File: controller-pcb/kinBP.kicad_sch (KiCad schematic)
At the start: 33 parts, among them J1 LEFT_TOP, J10 LEFT_THUMB, J11 RIGHT_THUMB, J12 RIGHT_THUMB, J13 LEFT_THUMB, J14 Conn_02x04_Odd_Even, J15 USB Cable Socket, J2 LEFT_TOP, J3 RIGHT_TOP, J4 RIGHT_TOP, J5 RIGHT_KEYWELL, J6 LEFT_KEYWELL, J7 LEFT_THUMB, J8 RIGHT_THUMB, J9 Conn_02x04_Odd_Even, Q1 MMBT3904, Q2 MMBT3904, U1 weact_STM32F4x1

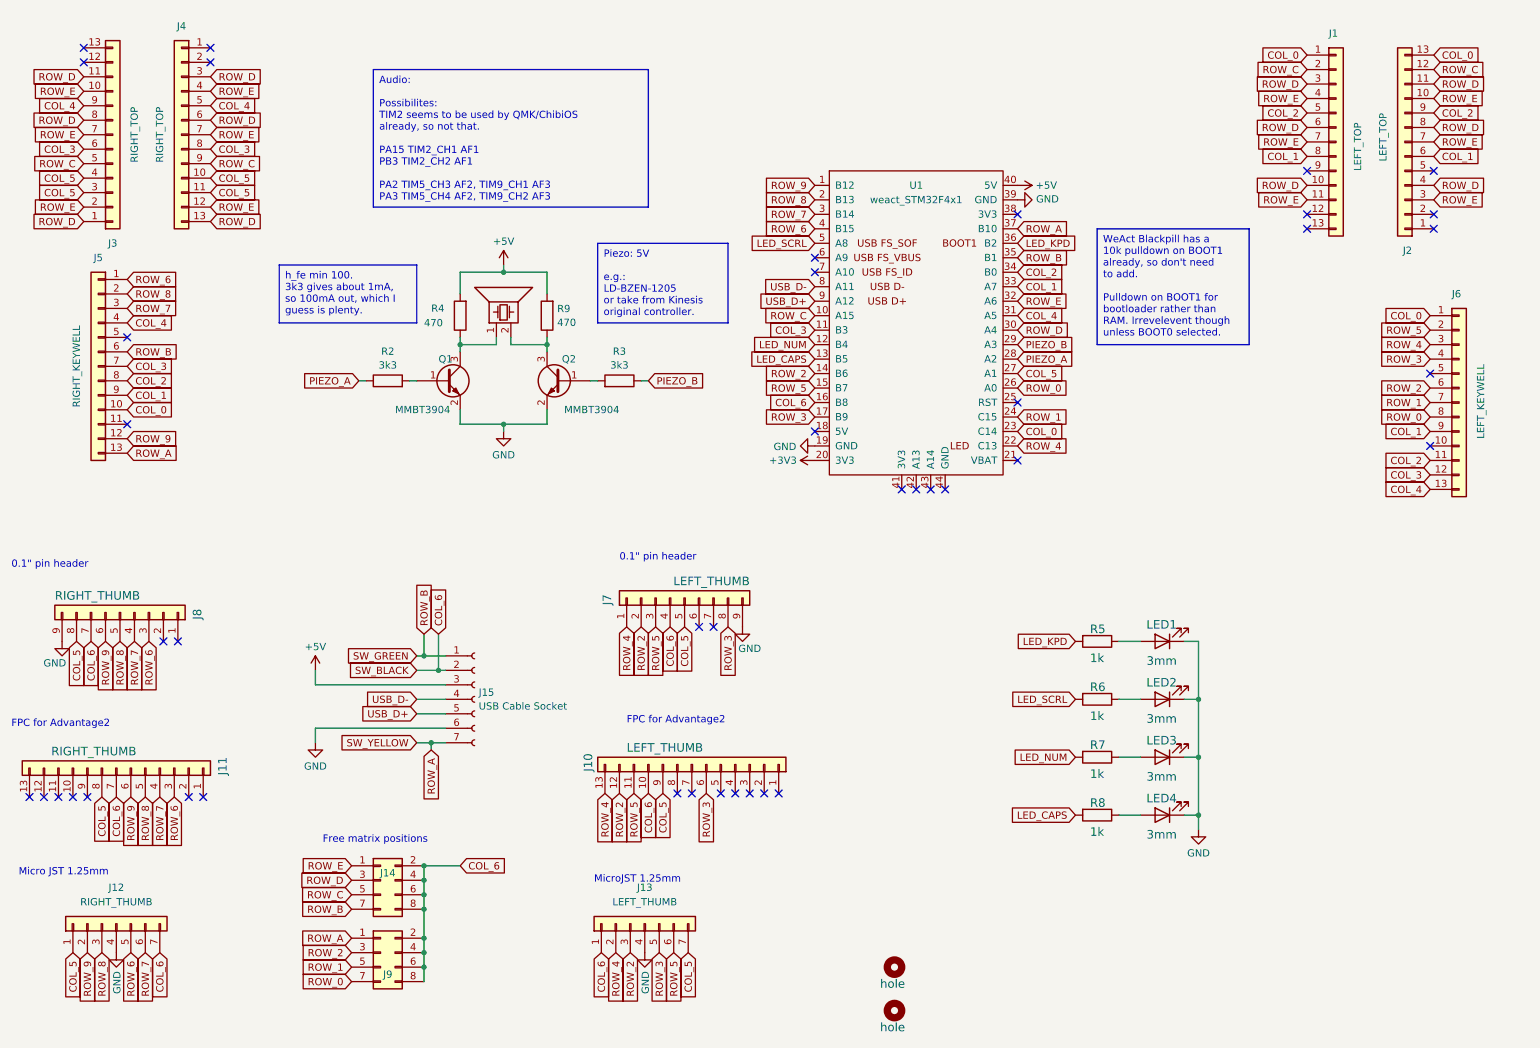
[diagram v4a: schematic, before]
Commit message: Added 10pin ARM Cortex debug header.
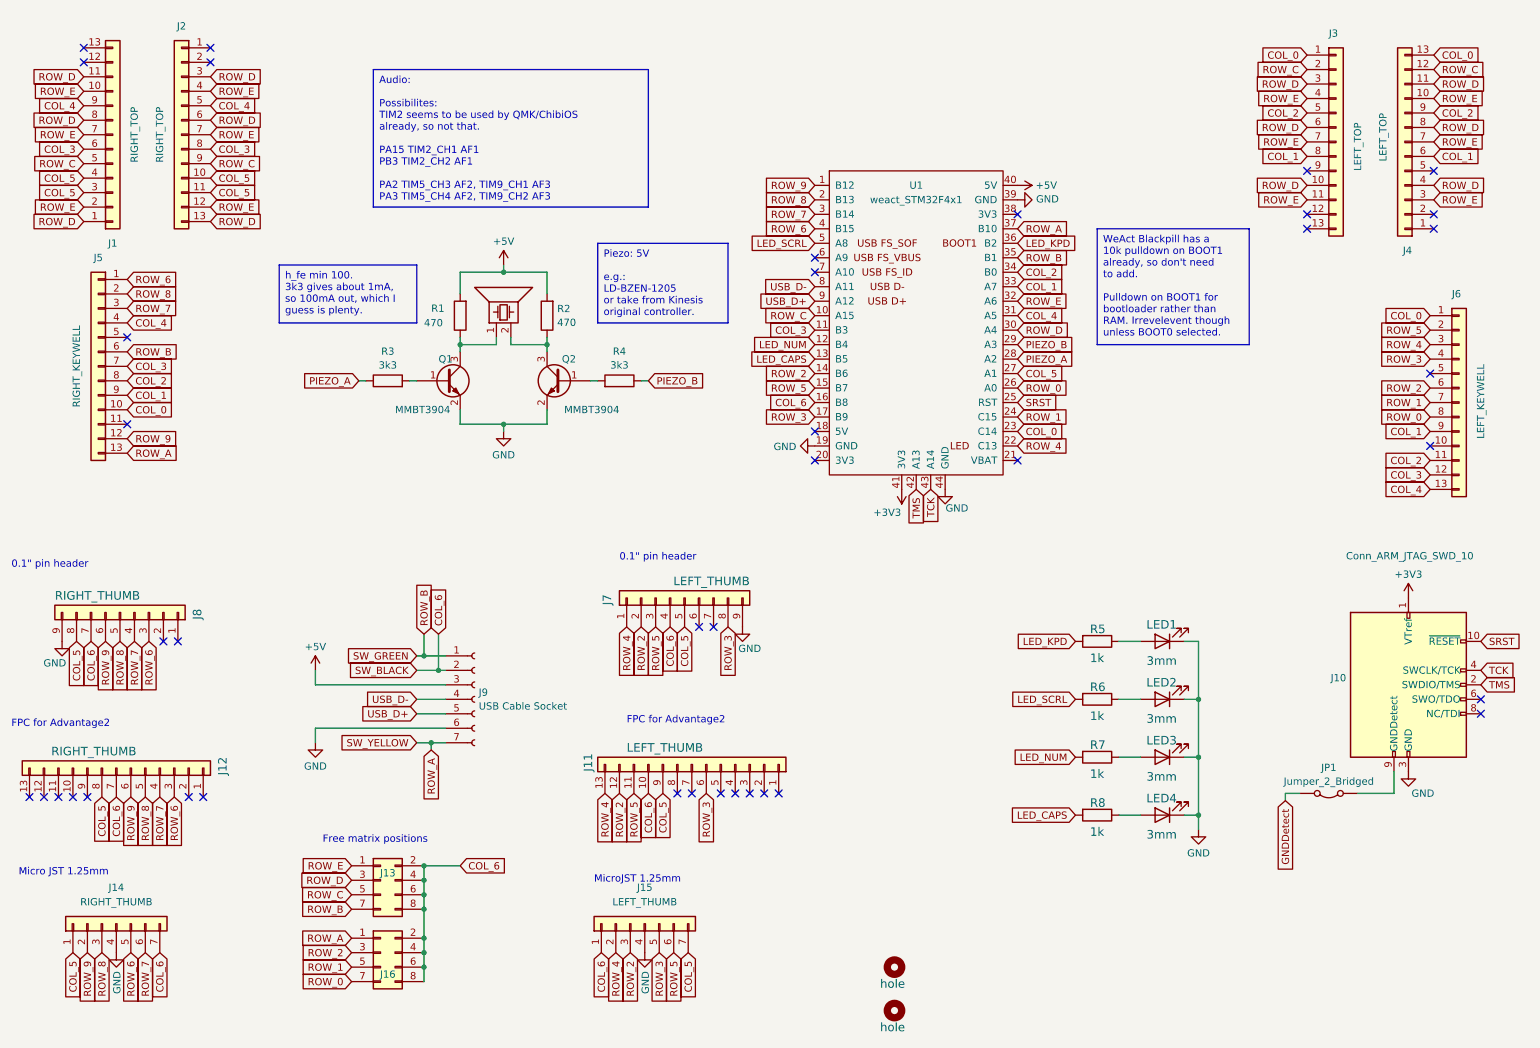
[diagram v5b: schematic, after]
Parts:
- added J10: Conn_ARM_JTAG_SWD_10, river:CONN_3220-10-0100-00_CNC, symbol Connector:Conn_ARM_JTAG_SWD_10
- added JP1: Jumper_2_Bridged, Jumper:SolderJumper-2_P1.3mm_Bridged2Bar_Pad1.0x1.5mm, symbol Jumper:Jumper_2_Bridged
- renumbered J3 to J1, J10 to J11, J11 to J12, J14 to J13, J12 to J14, J13 to J15, J9 to J16, J4 to J2, J1 to J3, J2 to J4, J15 to J9, R4 to R1, R9 to R2, R2 to R3, R3 to R4
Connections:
- net +3V3: now also U1.41 (3V3), J10.1 (VTref); no longer U1.20 (3V3)
- net GND: now also U1.44 (GND), J10.3 (GND), J10.5 (GND)
- net SRST: now reaches U1.25 (RST)
- net SRST: now also J10.10 (~{RESET})
- net TMS: now reaches U1.42 (A13)
- net TMS: now also J10.2 (SWDIO/TMS)
- net TCK: now reaches U1.43 (A14)
- net TCK: now also J10.4 (SWCLK/TCK)
- new net: J10.9 (GNDDetect), JP1.1 (A)
- new net GNDDetect: JP1.2 (B)
- no-connect marks 42 -> 40
